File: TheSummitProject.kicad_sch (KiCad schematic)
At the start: 32 parts, among them IC1 STM32U5F7VJT6, J1 Cortex SWD, J2 USB C, SW1 SW_SPDT, U2 USBLC6-2SC6, U3 USBLC6-2SC6, Y1 16Mhz, Y2 32.768Khz

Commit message: added peripherals pins
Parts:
- added R19, R20, R21: R, symbol Device:R
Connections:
- net +3.3V: now also R19.1, R20.1, R21.1
- net GPS_TX: now reaches IC1.15 (GPS_RX)
- net GPS_RX: now reaches IC1.16 (GPS_TX)
- net LoRa_TX: now reaches IC1.23 (LoRa_TX)
- net LoRa_RX: now reaches IC1.24 (LoRa_RX)
- net LSM303_XL_CS: now reaches IC1.33 (LSM303_XL_CS)
- net LSM303_XL_CS: now also R19.2
- net LSM303_MAG_CS: now reaches IC1.34 (LSM303_MAG_CS)
- net LSM303_MAG_CS: now also R20.2
- net BME280_CS: now reaches IC1.35 (BME280_CS)
- net BME280_CS: now also R21.2
- net RCC_MCO: now reaches IC1.67 (RCC_MCO)
- net SNSR_MOSI: now reaches IC1.87 (SNSR_MOSI)
- net SNSR_SCK: now reaches IC1.89 (SNSR_SCK)
- net SNSR_MISO: now reaches IC1.90 (SNSR_MISO)

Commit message: added resistance to CS pins
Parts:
- C1, C10, C11, C13, C14, C15, C16, C17, C18, C19, C2, C23, C3, C4, C5, C6, C7, C9: footprint (none) -> Capacitor_SMD:C_0603_1608Metric
- C12, C8: footprint (none) -> Capacitor_SMD:C_0805_2012Metric
- C24: footprint (none) -> Capacitor_SMD:C_1812_4532Metric
- FB1: footprint (none) -> Inductor_SMD:L_0603_1608Metric
- J1: footprint (none) -> Connector_PinHeader_2.54mm:PinHeader_2x05_P2.54mm_Vertical
- J2: footprint (none) -> Connector_USB:USB_C_Receptacle_GCT_USB4085
- R1, R5: footprint (none) -> Resistor_SMD:R_0603_1608Metric
- R19, R20, R21: value R -> 4.7k
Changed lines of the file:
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@@
 			)
 		)
-		(property "Footprint" ""
+		(property "Footprint" "Capacitor_SMD:C_0603_1608Metric"
 			(at 197.8152 53.34 0)
 			(hide yes)
@@
 			)
 		)
-		(property "Footprint" ""
+		(property "Footprint" "Capacitor_SMD:C_0603_1608Metric"
 			(at 173.6852 53.34 0)
 			(hide yes)
@@
 			)
 		)
-		(property "Footprint" ""
+		(property "Footprint" "Capacitor_SMD:C_0603_1608Metric"
 			(at 248.6152 53.34 0)
 			(hide yes)
@@
 			)
 		)
-		(property "Footprint" ""
+		(property "Footprint" "Capacitor_SMD:C_0603_1608Metric"
 			(at 46.6852 125.73 0)
 			(hide yes)
@@
 			)
 		)
-		(property "Footprint" ""
+		(property "Footprint" "Capacitor_SMD:C_0603_1608Metric"
 			(at 22.5552 99.06 0)
 			(hide yes)
@@
 			)
 		)
-		(property "Value" "R"
+		(property "Value" "4.7k"
 			(at 80.01 185.42 90)
 			(show_name no)
@@
 			)
 		)
-		(property "Footprint" ""
+		(property "Footprint" "Resistor_SMD:R_0603_1608Metric"
 			(at 70.612 35.56 90)
 			(hide yes)
@@
 			)
 		)
-		(property "Footprint" ""
+		(property "Footprint" "Capacitor_SMD:C_0603_1608Metric"
 			(at 35.2552 66.04 0)
 			(hide yes)
@@
 			)
 		)
-		(property "Footprint" ""
+		(property "Footprint" "Capacitor_SMD:C_0603_1608Metric"
 			(at 223.2152 53.34 0)
 			(hide yes)
@@
 			)
 		)
-		(property "Footprint" ""
+		(property "Footprint" "Capacitor_SMD:C_0603_1608Metric"
 			(at 194.0052 123.19 0)
 			(hide yes)
@@
 			)
 		)
-		(property "Footprint" ""
+		(property "Footprint" "Capacitor_SMD:C_0603_1608Metric"
 			(at 194.0052 82.55 0)
 			(hide yes)
@@
 			)
 		)
-		(property "Footprint" ""
+		(property "Footprint" "Capacitor_SMD:C_0603_1608Metric"
 			(at 235.9152 67.31 0)
 			(hide yes)
@@
 			)
 		)
-		(property "Value" "R"
+		(property "Value" "4.7k"
 			(at 80.01 177.8 90)
 			(show_name no)
@@
 			)
 		)
-		(property "Footprint" ""
+		(property "Footprint" "Connector_PinHeader_2.54mm:PinHeader_2x05_P2.54mm_Vertical"
 			(at 148.59 55.88 0)
 			(hide yes)
@@
 			)
 		)
-		(property "Footprint" ""
+		(property "Footprint" "Capacitor_SMD:C_0603_1608Metric"
 			(at 210.5152 53.34 0)
 			(hide yes)
@@
 			)
 		)
-		(property "Footprint" ""
+		(property "Footprint" "Inductor_SMD:L_0603_1608Metric"
 			(at 207.01 73.152 90)
 			(hide yes)
@@
 			)
 		)
-		(property "Footprint" ""
+		(property "Footprint" "Capacitor_SMD:C_0603_1608Metric"
 			(at 186.3852 53.34 0)
 			(hide yes)
@@
 			)
 		)
-		(property "Footprint" ""
+		(property "Footprint" "Connector_USB:USB_C_Receptacle_GCT_USB4085"
 			(at 234.95 130.81 0)
 			(hide yes)
@@
 			)
 		)
-		(property "Footprint" ""
+		(property "Footprint" "Capacitor_SMD:C_0603_1608Metric"
 			(at 235.9152 53.34 0)
 			(hide yes)
@@
 			)
 		)
-		(property "Value" "R"
+		(property "Value" "4.7k"
 			(at 80.01 193.294 90)
 			(show_name no)
@@
 			)
 		)
-		(property "Footprint" ""
+		(property "Footprint" "Resistor_SMD:R_0603_1608Metric"
 			(at 263.652 104.14 90)
 			(hide yes)
@@
 			)
 		)
-		(property "Footprint" ""
+		(property "Footprint" "Capacitor_SMD:C_0805_2012Metric"
 			(at 123.19 184.4548 0)
 			(hide yes)
@@
 			)
 		)
-		(property "Footprint" ""
+		(property "Footprint" "Capacitor_SMD:C_0603_1608Metric"
 			(at 33.9852 99.06 0)
 			(hide yes)
@@
 			)
 		)
-		(property "Footprint" ""
+		(property "Footprint" "Capacitor_SMD:C_0805_2012Metric"
 			(at 262.5852 53.34 0)
 			(hide yes)
@@
 			)
 		)
-		(property "Footprint" ""
+		(property "Footprint" "Capacitor_SMD:C_0603_1608Metric"
 			(at 23.8252 66.04 0)
 			(hide yes)
@@
 			)
 		)
-		(property "Footprint" ""
+		(property "Footprint" "Capacitor_SMD:C_1812_4532Metric"
 			(at 254.3048 100.33 0)
 			(hide yes)
@@
 			)
 		)
-		(property "Footprint" ""
+		(property "Footprint" "Capacitor_SMD:C_0603_1608Metric"
 			(at 219.4052 82.55 0)
 			(hide yes)
@@
 			)
 		)
-		(property "Footprint" ""
+		(property "Footprint" "Capacitor_SMD:C_0603_1608Metric"
 			(at 230.8352 82.55 0)
 			(hide yes)
@@
 			)
 		)
-		(property "Footprint" ""
+		(property "Footprint" "Capacitor_SMD:C_0603_1608Metric"
 			(at 224.4852 67.31 0)
 			(hide yes)

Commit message: assigned footprint and created PCB file
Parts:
- R19, R20, R21: footprint (none) -> Resistor_SMD:R_0603_1608Metric
- SW1: footprint (none) -> Button_Switch_SMD:SW_Push_1P1T-SH_NO_CK_KMR2xxG
- Y1: footprint (none) -> Crystal:Crystal_SMD_5032-4Pin_5.0x3.2mm
- Y2: footprint (none) -> Crystal:Crystal_SMD_3225-4Pin_3.2x2.5mm
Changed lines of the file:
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@@
 			)
 		)
-		(property "Footprint" ""
+		(property "Footprint" "Resistor_SMD:R_0603_1608Metric"
 			(at 80.01 189.738 90)
 			(hide yes)
@@
 			)
 		)
-		(property "Footprint" ""
+		(property "Footprint" "Crystal:Crystal_SMD_5032-4Pin_5.0x3.2mm"
 			(at 24.13 109.22 0)
 			(hide yes)
@@
 			)
 		)
-		(property "Footprint" ""
+		(property "Footprint" "Crystal:Crystal_SMD_3225-4Pin_3.2x2.5mm"
 			(at 25.4 76.2 0)
 			(hide yes)
@@
 			)
 		)
-		(property "Footprint" ""
+		(property "Footprint" "Resistor_SMD:R_0603_1608Metric"
 			(at 80.01 182.118 90)
 			(hide yes)
@@
 			)
 		)
-		(property "Footprint" ""
+		(property "Footprint" "Resistor_SMD:R_0603_1608Metric"
 			(at 80.01 197.358 90)
 			(hide yes)
@@
 			)
 		)
-		(property "Footprint" ""
+		(property "Footprint" "Button_Switch_SMD:SW_Push_1P1T-SH_NO_CK_KMR2xxG"
 			(at 78.74 25.4 0)
 			(hide yes)

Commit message: Updated footprints fixed DRC errors
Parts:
- SW1: footprint Button_Switch_SMD:SW_Push_1P1T-SH_NO_CK_KMR2xxG -> Button_Switch_SMD:SW_SPDT_CK_JS102011SAQN
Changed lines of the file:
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@@
 			)
 		)
-		(property "Footprint" "Button_Switch_SMD:SW_Push_1P1T-SH_NO_CK_KMR2xxG"
+		(property "Footprint" "Button_Switch_SMD:SW_SPDT_CK_JS102011SAQN"
 			(at 78.74 25.4 0)
 			(hide yes)

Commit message: Changed pcb to 4 layers and completed 50% traces
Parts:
- renumbered J2 to USB-C1
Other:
- moved on the sheet: C18
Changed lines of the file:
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@@
 		(dnp no)
 		(fields_autoplaced yes)
-		(property "Reference" "J2"
+		(property "Reference" "USB-C1"
 			(at 250.19 129.5399 0)
 			(show_name no)
@@
 			(project "TheSummitProject"
 				(path "/824a843c-f98d-42ac-aedf-08925675716b"
-					(reference "J2")
+					(reference "USB-C1")
 					(unit 1)
 				)
@@
 	(symbol
 		(lib_id "Device:C")
-		(at 223.52 71.12 0)
-		(mirror x)
-		(unit 1)
-		(body_style 1)
-		(exclude_from_sim no)
-		(in_bom yes)
-		(on_board yes)
-		(in_pos_files yes)
-		(dnp no)
-		(fields_autoplaced yes)
+		(at 223.52 71.12 180)
+		(unit 1)
+		(body_style 1)
+		(exclude_from_sim no)
+		(in_bom yes)
+		(on_board yes)
+		(in_pos_files yes)
+		(dnp no)
 		(property "Reference" "C18"
-			(at 227.33 72.3901 0)
+			(at 219.71 72.3901 0)
 			(show_name no)
 			(do_not_autoplace no)
@@
 		)
 		(property "Value" "1u"
-			(at 227.33 69.8501 0)
+			(at 219.71 69.8501 0)
 			(show_name no)
 			(do_not_autoplace no)
@@
 		)
 		(property "Footprint" "Capacitor_SMD:C_0603_1608Metric"
-			(at 224.4852 67.31 0)
-			(hide yes)
-			(show_name no)
+			(at 222.5548 67.31 0)
+			(hide yes)
+			(show_name no)

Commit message: Changed usbc footprint
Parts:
- USB-C1: footprint Connector_USB:USB_C_Receptacle_GCT_USB4085 -> Connector_USB:USB_C_Receptacle_GCT_USB4105-xx-A_16P_TopMnt_Horizontal
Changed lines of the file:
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@@
 			)
 		)
-		(property "Footprint" "Connector_USB:USB_C_Receptacle_GCT_USB4085"
+		(property "Footprint" "Connector_USB:USB_C_Receptacle_GCT_USB4105-xx-A_16P_TopMnt_Horizontal"
 			(at 234.95 130.81 0)
 			(hide yes)

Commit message: Added data for pcb fab
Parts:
- IC1: Height 1.6 -> (none)

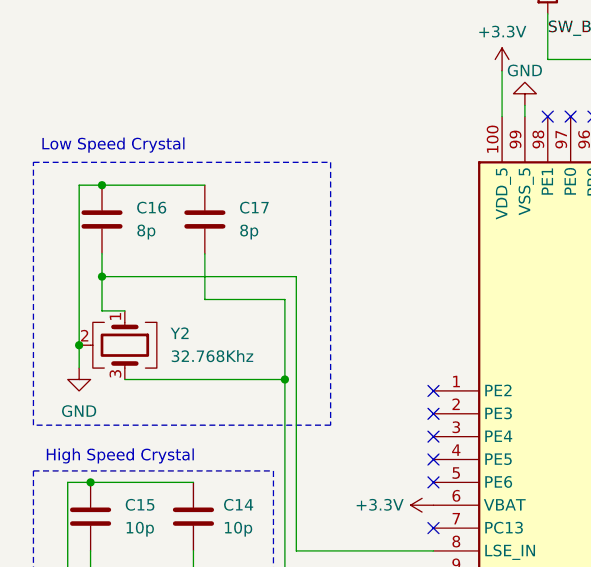
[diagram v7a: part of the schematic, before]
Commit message: Updated footprint of 32.768k crystal to 3215
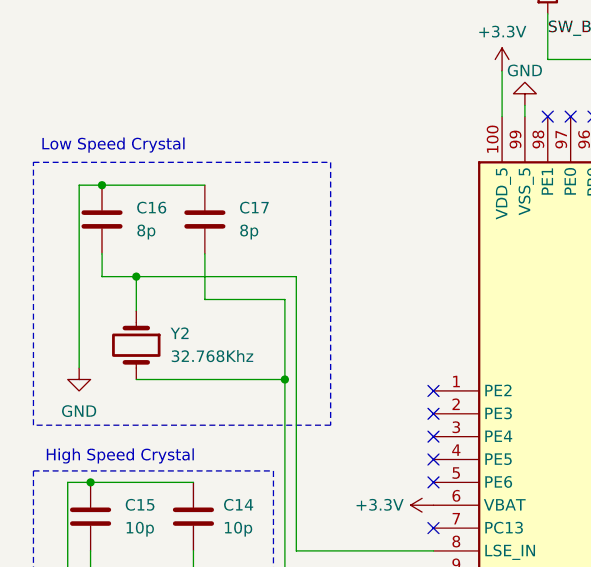
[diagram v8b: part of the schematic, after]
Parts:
- Y2: footprint Crystal:Crystal_SMD_3225-4Pin_3.2x2.5mm -> Crystal:Crystal_SMD_3215-2Pin_3.2x1.5mm; symbol Device:Crystal_GND24 -> Device:Crystal
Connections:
- net GND: no longer Y2.2 (G), Y2.4 (G)
- net at C17.2, IC1.9 (LSE_OUT): now also Y2.2; no longer Y2.3
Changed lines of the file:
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@@
 	)
 	(junction
+		(at 26.67 68.58)
+		(diameter 0)
+		(color 0 0 0 0)
+	)
+	(junction
 		(at 198.12 130.81)
 		(diameter 0)
@@
 	)
 	(junction
+		(at 43.18 80.01)
+		(diameter 0)
+		(color 0 0 0 0)
+	)
+	(junction
 		(at 205.74 147.32)
 		(diameter 0)
@@
 	)
 	(junction
-		(at 22.86 68.58)
-		(diameter 0)
-		(color 0 0 0 0)
-	)
-	(junction
 		(at 196.85 123.19)
 		(diameter 0)
@@
 	)
 	(junction
-		(at 20.32 76.2)
-		(diameter 0)
-		(color 0 0 0 0)
-	)
-	(junction
 		(at 222.25 146.05)
 		(diameter 0)
@@
 	)
 	(junction
-		(at 43.18 80.01)
-		(diameter 0)
-		(color 0 0 0 0)
-	)
-	(junction
 		(at 196.85 53.34)
 		(diameter 0)
@@
 	(wire
 		(pts
-			(xy 20.32 76.2) (xy 20.32 58.42)
+			(xy 20.32 58.42) (xy 20.32 78.74)
 		)
 		(stroke
@@
 	(wire
 		(pts
-			(xy 22.86 72.39) (xy 25.4 72.39)
-		)
-		(stroke
-			(width 0)
-			(type default)
-		)
-	)
-	(wire
-		(pts
 			(xy 198.12 130.81) (xy 198.12 147.32)
 		)
@@
 	(wire
 		(pts
-			(xy 25.4 80.01) (xy 43.18 80.01)
+			(xy 26.67 80.01) (xy 43.18 80.01)
 		)
 		(stroke
@@
 	(wire
 		(pts
-			(xy 22.86 68.58) (xy 44.45 68.58)
-		)
-		(stroke
-			(width 0)
-			(type default)
-		)
-	)
-	(wire
-		(pts
 			(xy 36.83 104.14) (xy 36.83 113.03)
 		)
@@
 	(wire
 		(pts
+			(xy 26.67 68.58) (xy 44.45 68.58)
+		)
+		(stroke
+			(width 0)
+			(type default)
+		)
+	)
+	(wire
+		(pts
+			(xy 26.67 68.58) (xy 22.86 68.58)
+		)
+		(stroke
+			(width 0)
+			(type default)
+		)
+	)
+	(wire
+		(pts
 			(xy 238.76 106.68) (xy 238.76 107.95)
 		)
@@
 	(wire
 		(pts
-			(xy 20.32 78.74) (xy 20.32 76.2)
-		)
-		(stroke
-			(width 0)
-			(type default)
-		)
-	)
-	(wire
-		(pts
 			(xy 133.35 53.34) (xy 143.51 53.34)
 		)
@@
 	(wire
 		(pts
-			(xy 22.86 68.58) (xy 22.86 72.39)
+			(xy 26.67 68.58) (xy 26.67 72.39)
 		)
 		(stroke
@@
 			)
 		)
-		(property "HEIGHT" "1.6"
-			(at 132.08 453.34 0)
-			(hide yes)
-			(show_name no)
-			(do_not_autoplace no)
-			(effects
-				(font
-					(size 1.27 1.27)
-				)
-				(justify left top)
-			)
-		)
 		(property "KLC_S3.3" ""
 			(at 59.69 81.28 0)
@@
 	)
 	(symbol
-		(lib_id "Device:Crystal_GND24")
-		(at 25.4 76.2 270)
+		(lib_id "Device:Crystal")
+		(at 26.67 76.2 270)
 		(unit 1)
 		(body_style 1)
@@
 			)
 		)
-		(property "Footprint" "Crystal:Crystal_SMD_3225-4Pin_3.2x2.5mm"
-			(at 25.4 76.2 0)
+		(property "Footprint" "Crystal:Crystal_SMD_3215-2Pin_3.2x1.5mm"
+			(at 26.67 76.2 0)
 			(hide yes)
 			(show_name no)
@@
 		)
 		(property "Datasheet" ""
-			(at 25.4 76.2 0)
+			(at 26.67 76.2 0)
 			(hide yes)
 			(show_name no)
@@
 			)
 		)
-		(property "Description" "Four pin crystal, GND on pins 2 and 4"
-			(at 25.4 76.2 0)
+		(property "Description" "Two pin crystal"
+			(at 26.67 76.2 0)
 			(hide yes)
 			(show_name no)
@@
 		)
 		(property private "KLC_S3.3" "The rectangle is not a symbol body but a graphical element"
-			(at 12.7 76.2 0)
+			(at 13.97 76.2 0)
 			(hide yes)
 			(show_name yes)
@@
 		)
 		(property private "KLC_S4.1" "Some pins are on 50mil grid to make the symbol small"
-			(at 10.16 76.2 0)
+			(at 11.43 76.2 0)
 			(hide yes)
 			(show_name yes)
@@
 		(pin "1"
 		)
-		(pin "3"
-		)
-		(pin "4"
-		)
 		(instances
